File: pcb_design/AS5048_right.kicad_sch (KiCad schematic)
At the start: 6 parts

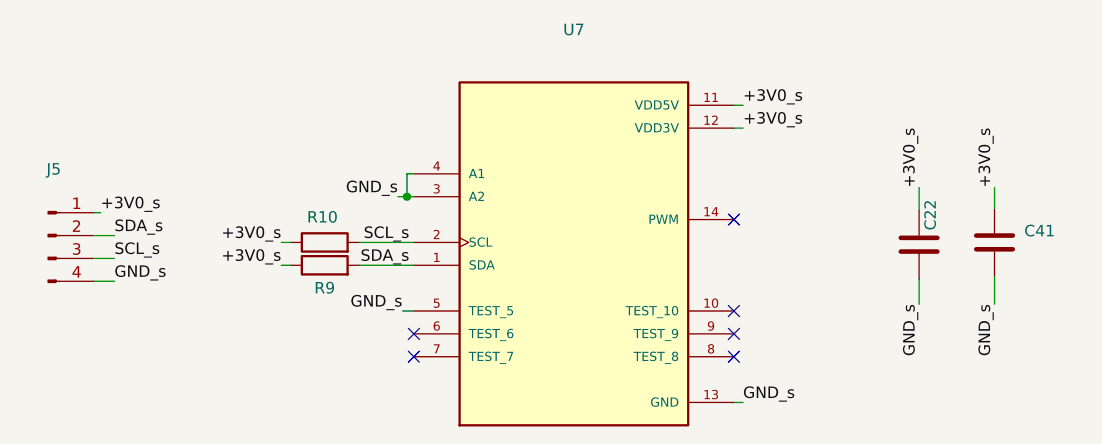
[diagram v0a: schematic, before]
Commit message: Add resistors between MOSFET gate
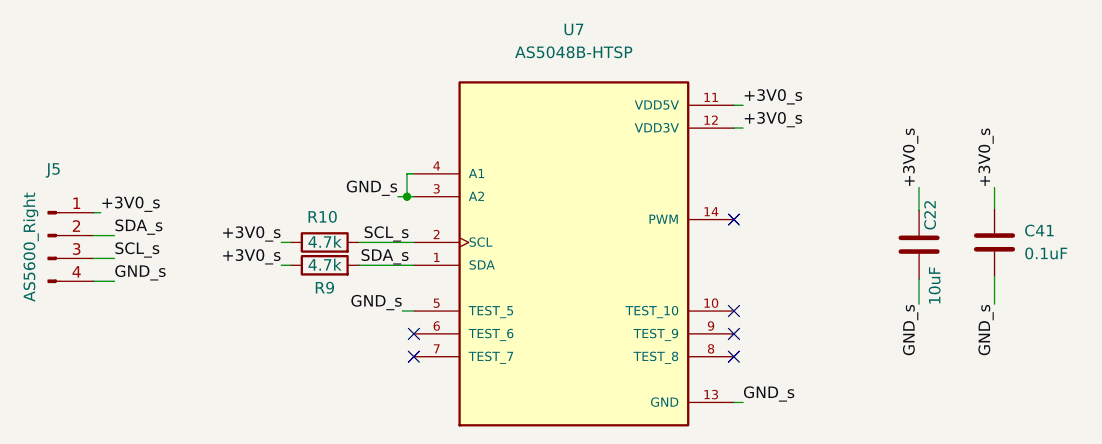
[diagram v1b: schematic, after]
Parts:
- C22: value (none) -> 10uF; footprint (none) -> Capacitor_SMD:C_0603_1608Metric
- C41: value (none) -> 0.1uF; footprint (none) -> Capacitor_SMD:C_0402_1005Metric
- J5: value (none) -> AS5600_Right; footprint (none) -> mushak_mount_footprint:STAND_SLAVE_04
- R10, R9: value (none) -> 4.7k; footprint (none) -> Resistor_SMD:R_0402_1005Metric
- U7: value (none) -> AS5048B-HTSP; footprint (none) -> AS5048B-HTSP:SOP65P640X120-14N
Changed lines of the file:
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@@
       (effects (font (size 1.27 1.27)) (justify left))
     )
-    (property "Value" "" (id 1) (at 213.36 99.3139 0)
+    (property "Value" "0.1uF" (id 1) (at 213.36 99.3139 0)
       (effects (font (size 1.27 1.27)) (justify left))
     )
-    (property "Footprint" "" (id 2) (at 211.0232 101.854 0)
+    (property "Footprint" "Capacitor_SMD:C_0402_1005Metric" (id 2) (at 211.0232 101.854 0)
       (effects (font (size 1.27 1.27)) hide)
     )
@@
     (in_bom yes) (on_board yes)
     (property "Reference" "C22" (id 0) (at 202.946 94.996 90))
-    (property "Value" "" (id 1) (at 203.454 102.87 90))
-    (property "Footprint" "" (id 2) (at 200.7108 94.488 0)
+    (property "Value" "10uF" (id 1) (at 203.454 102.87 90))
+    (property "Footprint" "Capacitor_SMD:C_0603_1608Metric" (id 2) (at 200.7108 94.488 0)
       (effects (font (size 1.27 1.27)) hide)
     )
@@
     (in_bom yes) (on_board yes) (fields_autoplaced)
     (property "Reference" "U7" (id 0) (at 163.322 74.422 0))
-    (property "Value" "" (id 1) (at 163.322 76.962 0))
-    (property "Footprint" "" (id 2) (at 163.322 98.044 0)
+    (property "Value" "AS5048B-HTSP" (id 1) (at 163.322 76.962 0))
+    (property "Footprint" "AS5048B-HTSP:SOP65P640X120-14N" (id 2) (at 163.322 98.044 0)
       (effects (font (size 1.27 1.27)) (justify left bottom) hide)
     )
@@
     (in_bom yes) (on_board yes)
     (property "Reference" "R10" (id 0) (at 135.382 95.25 90))
-    (property "Value" "" (id 1) (at 135.636 98.044 90))
-    (property "Footprint" "" (id 2) (at 135.636 99.822 90)
+    (property "Value" "4.7k" (id 1) (at 135.636 98.044 90))
+    (property "Footprint" "Resistor_SMD:R_0402_1005Metric" (id 2) (at 135.636 99.822 90)
       (effects (font (size 1.27 1.27)) hide)
     )
@@
     (in_bom yes) (on_board yes)
     (property "Reference" "R9" (id 0) (at 135.636 103.124 90))
-    (property "Value" "" (id 1) (at 135.636 100.584 90))
-    (property "Footprint" "" (id 2) (at 135.636 102.362 90)
+    (property "Value" "4.7k" (id 1) (at 135.636 100.584 90))
+    (property "Footprint" "Resistor_SMD:R_0402_1005Metric" (id 2) (at 135.636 102.362 90)
       (effects (font (size 1.27 1.27)) hide)
     )
@@
     (in_bom yes) (on_board yes)
     (property "Reference" "J5" (id 0) (at 105.537 89.916 0))
-    (property "Value" "" (id 1) (at 102.87 98.552 90))
-    (property "Footprint" "" (id 2) (at 104.902 97.282 0)
+    (property "Value" "AS5600_Right" (id 1) (at 102.87 98.552 90))
+    (property "Footprint" "mushak_mount_footprint:STAND_SLAVE_04" (id 2) (at 104.902 97.282 0)
       (effects (font (size 1.27 1.27)) hide)
     )

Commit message: modified capacitors for encoders
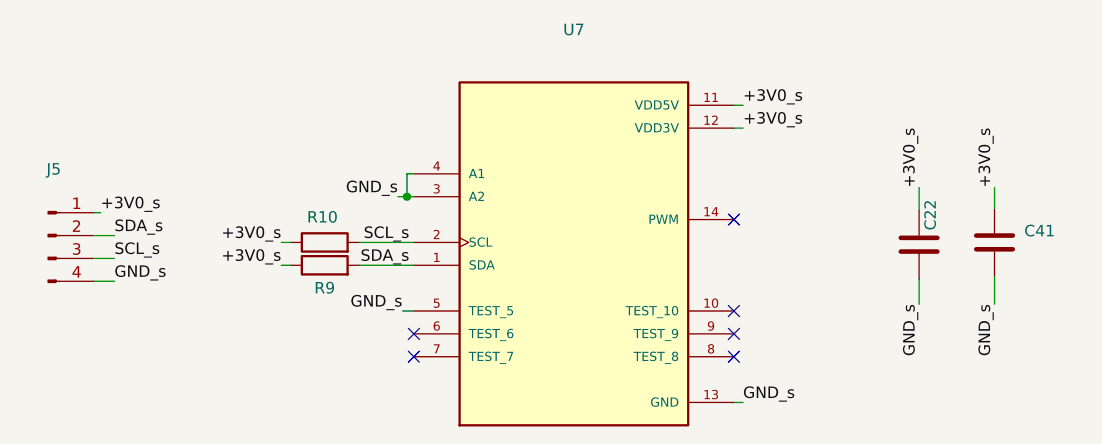
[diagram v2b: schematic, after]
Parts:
- C22: value 10uF -> (none); footprint Capacitor_SMD:C_0603_1608Metric -> (none)
- C41: value 0.1uF -> (none); footprint Capacitor_SMD:C_0402_1005Metric -> (none)
- J5: value AS5600_Right -> (none); footprint mushak_mount_footprint:STAND_SLAVE_04 -> (none)
- R10, R9: value 4.7k -> (none); footprint Resistor_SMD:R_0402_1005Metric -> (none)
- U7: value AS5048B-HTSP -> (none); footprint AS5048B-HTSP:SOP65P640X120-14N -> (none)
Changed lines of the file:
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@@
       (effects (font (size 1.27 1.27)) (justify left))
     )
-    (property "Value" "0.1uF" (id 1) (at 213.36 99.3139 0)
+    (property "Value" "" (id 1) (at 213.36 99.3139 0)
       (effects (font (size 1.27 1.27)) (justify left))
     )
-    (property "Footprint" "Capacitor_SMD:C_0402_1005Metric" (id 2) (at 211.0232 101.854 0)
+    (property "Footprint" "" (id 2) (at 211.0232 101.854 0)
       (effects (font (size 1.27 1.27)) hide)
     )
@@
     (in_bom yes) (on_board yes)
     (property "Reference" "C22" (id 0) (at 202.946 94.996 90))
-    (property "Value" "10uF" (id 1) (at 203.454 102.87 90))
-    (property "Footprint" "Capacitor_SMD:C_0603_1608Metric" (id 2) (at 200.7108 94.488 0)
+    (property "Value" "" (id 1) (at 203.454 102.87 90))
+    (property "Footprint" "" (id 2) (at 200.7108 94.488 0)
       (effects (font (size 1.27 1.27)) hide)
     )
@@
     (in_bom yes) (on_board yes) (fields_autoplaced)
     (property "Reference" "U7" (id 0) (at 163.322 74.422 0))
-    (property "Value" "AS5048B-HTSP" (id 1) (at 163.322 76.962 0))
-    (property "Footprint" "AS5048B-HTSP:SOP65P640X120-14N" (id 2) (at 163.322 98.044 0)
+    (property "Value" "" (id 1) (at 163.322 76.962 0))
+    (property "Footprint" "" (id 2) (at 163.322 98.044 0)
       (effects (font (size 1.27 1.27)) (justify left bottom) hide)
     )
@@
     (in_bom yes) (on_board yes)
     (property "Reference" "R10" (id 0) (at 135.382 95.25 90))
-    (property "Value" "4.7k" (id 1) (at 135.636 98.044 90))
-    (property "Footprint" "Resistor_SMD:R_0402_1005Metric" (id 2) (at 135.636 99.822 90)
+    (property "Value" "" (id 1) (at 135.636 98.044 90))
+    (property "Footprint" "" (id 2) (at 135.636 99.822 90)
       (effects (font (size 1.27 1.27)) hide)
     )
@@
     (in_bom yes) (on_board yes)
     (property "Reference" "R9" (id 0) (at 135.636 103.124 90))
-    (property "Value" "4.7k" (id 1) (at 135.636 100.584 90))
-    (property "Footprint" "Resistor_SMD:R_0402_1005Metric" (id 2) (at 135.636 102.362 90)
+    (property "Value" "" (id 1) (at 135.636 100.584 90))
+    (property "Footprint" "" (id 2) (at 135.636 102.362 90)
       (effects (font (size 1.27 1.27)) hide)
     )
@@
     (in_bom yes) (on_board yes)
     (property "Reference" "J5" (id 0) (at 105.537 89.916 0))
-    (property "Value" "AS5600_Right" (id 1) (at 102.87 98.552 90))
-    (property "Footprint" "mushak_mount_footprint:STAND_SLAVE_04" (id 2) (at 104.902 97.282 0)
+    (property "Value" "" (id 1) (at 102.87 98.552 90))
+    (property "Footprint" "" (id 2) (at 104.902 97.282 0)
       (effects (font (size 1.27 1.27)) hide)
     )
